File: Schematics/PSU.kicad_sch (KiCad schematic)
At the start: 59 parts

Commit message: - Updated current libraries - New 7 inc display with ESP32S3 and second USB upload port - Start of I2C feeder interface slave on display.
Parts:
- gave numbers to parts that had none: 59

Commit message: updated schematics.
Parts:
- J44: value Upper Cannon -> Upper Cannon
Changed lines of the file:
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@@
 			)
 		)
-		(property "Value" "Upper Cannon "
+		(property "Value" "Upper Cannon"
 			(at 190.5 22.86 90)
 			(effects

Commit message: Upgreade byte value interface to short.  First stage of refactoring midi input for rotory encoders.  Still needs scaling.
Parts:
- renumbered C67 to C115, C71 to C116, C64 to C117, C68 to C118, C72 to C119, C65 to C120, C69 to C121, C73 to C122, C66 to C123, C70 to C124, C74 to C125, D17 to D10, D13 to D11, D16 to D12, D19 to D13, D12 to D5, D15 to D6, D18 to D7, D11 to D8, D14 to D9, J44 to J55, J45 to J56, J46 to J57, J47 to J58, J48 to J59, J49 to J60, J50 to J61, J51 to J62, MES3 to MES2, MES6 to MES3, MES2 to MES4, MES4 to MES5, MES5 to MES6, R76 to R263, R77 to R264, RV3 to RV11, RV4 to RV12, RV5 to RV13, U23 to U73, U28 to U74, U34 to U75, U24 to U76, U26 to U77, U29 to U78, U31 to U79, U33 to U80, U35 to U81, U25 to U82, U27 to U83, U30 to U84, U32 to U85, U36 to U86

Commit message: Updated schematics including VCO and VCF daughter boards
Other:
- company:       MLE Tech                  Cedar Park, TX -> (none)
- title: Synth #2 -> Primary Power Supply
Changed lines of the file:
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@@
 	(paper "USLegal")
 	(title_block
-		(title "Synth #2")
-		(date "2023-07-27")
-		(rev "0.1")
-		(company "      MLE Tech                  Cedar Park, TX")
-		(comment 2 "In Development")
+		(title "Primary Power Supply")
+		(date "2025-01-16")
+		(rev "1.4")
+		(comment 1 "In Development ")
 	)
 	(junction

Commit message: Cleaned up page advance on display controls.
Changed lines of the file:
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@@
 (kicad_sch
-	(version 20231120)
+	(version 20250114)
 	(generator "eeschema")
-	(generator_version "8.0")
+	(generator_version "9.0")
 	(paper "USLegal")
 	(title_block
@@
 		(comment 1 "In Development ")
 	)
+	(text "Back Panel"
+		(exclude_from_sim no)
+		(at 35.3568 17.3482 0)
+		(effects
+			(font
+				(size 1.524 1.524)
+				(thickness 0.3048)
+				(bold yes)
+			)
+			(justify right bottom)
+		)
+	)
+	(text "LV300"
+		(exclude_from_sim no)
+		(at 30.48 83.185 0)
+		(effects
+			(font
+				(size 1.524 1.524)
+				(thickness 0.3048)
+				(bold yes)
+			)
+			(justify right bottom)
+		)
+	)
+	(text "Front Panel"
+		(exclude_from_sim no)
+		(at 162.56 53.34 0)
+		(effects
+			(font
+				(size 1.524 1.524)
+				(thickness 0.3048)
+				(bold yes)
+			)
+			(justify right bottom)
+		)
+	)
+	(text "Back Panel"
+		(exclude_from_sim no)
+		(at 210.82 17.78 0)
+		(effects
+			(font
+				(size 1.524 1.524)
+				(thickness 0.3048)
+				(bold yes)
+			)
+			(justify right bottom)
+		)
+	)
+	(text "Front Panel"
+		(exclude_from_sim no)
+		(at 257.81 60.96 0)
+		(effects
+			(font
+				(size 1.524 1.524)
+				(thickness 0.3048)
+				(bold yes)
+			)
+			(justify right bottom)
+		)
+	)
+	(text "LV30"
+		(exclude_from_sim no)
+		(at 30.4292 46.4566 0)
+		(effects
+			(font
+				(size 1.524 1.524)
+				(thickness 0.3048)
+				(bold yes)
+			)
+			(justify right bottom)
+		)
+	)
+	(text "Back Panel"
+		(exclude_from_sim no)
+		(at 97.6122 17.0942 0)
+		(effects
+			(font
+				(size 1.524 1.524)
+				(thickness 0.3048)
+				(bold yes)
+			)
+			(justify right bottom)
+		)
+	)
+	(text "LV300"
+		(exclude_from_sim no)
+		(at 30.1752 130.1496 0)
+		(effects
+			(font
+				(size 1.524 1.524)
+				(thickness 0.3048)
+				(bold yes)
+			)
+			(justify right bottom)
+		)
+	)
+	(text "Front Panel"
+		(exclude_from_sim no)
+		(at 61.8236 17.1196 0)
+		(effects
+			(font
+				(size 1.524 1.524)
+				(thickness 0.3048)
+				(bold yes)
+			)
+			(justify right bottom)
+		)
+	)
 	(junction
 		(at 77.47 161.29)
@@
 		)
 	)
-	(text "Back Panel"
-		(exclude_from_sim no)
-		(at 35.3568 17.3482 0)
-		(effects
-			(font
-				(size 1.524 1.524)
-				(thickness 0.3048)
-				(bold yes)
-			)
-			(justify right bottom)
-		)
-	)
-	(text "LV300"
-		(exclude_from_sim no)
-		(at 30.48 83.185 0)
-		(effects
-			(font
-				(size 1.524 1.524)
-				(thickness 0.3048)
-				(bold yes)
-			)
-			(justify right bottom)
-		)
-	)
-	(text "Front Panel"
-		(exclude_from_sim no)
-		(at 162.56 53.34 0)
-		(effects
-			(font
-				(size 1.524 1.524)
-				(thickness 0.3048)
-				(bold yes)
-			)
-			(justify right bottom)
-		)
-	)
-	(text "Back Panel"
-		(exclude_from_sim no)
-		(at 210.82 17.78 0)
-		(effects
-			(font
-				(size 1.524 1.524)
-				(thickness 0.3048)
-				(bold yes)
-			)
-			(justify right bottom)
-		)
-	)
-	(text "Front Panel"
-		(exclude_from_sim no)
-		(at 257.81 60.96 0)
-		(effects
-			(font
-				(size 1.524 1.524)
-				(thickness 0.3048)
-				(bold yes)
-			)
-			(justify right bottom)
-		)
-	)
-	(text "LV30"
-		(exclude_from_sim no)
-		(at 30.4292 46.4566 0)
-		(effects
-			(font
-				(size 1.524 1.524)
-				(thickness 0.3048)
-				(bold yes)
-			)
-			(justify right bottom)
-		)
-	)
-	(text "Back Panel"
-		(exclude_from_sim no)
-		(at 97.6122 17.0942 0)
-		(effects
-			(font
-				(size 1.524 1.524)
-				(thickness 0.3048)
-				(bold yes)
-			)
-			(justify right bottom)
-		)
-	)
-	(text "LV300"
-		(exclude_from_sim no)
-		(at 30.1752 130.1496 0)
-		(effects
-			(font
-				(size 1.524 1.524)
-				(thickness 0.3048)
-				(bold yes)
-			)
-			(justify right bottom)
-		)
-	)
-	(text "Front Panel"
-		(exclude_from_sim no)
-		(at 61.8236 17.1196 0)
-		(effects
-			(font
-				(size 1.524 1.524)
-				(thickness 0.3048)
-				(bold yes)
-			)
-			(justify right bottom)
-		)
-	)
 	(label "Brown"
 		(at 96.52 29.21 0)
-		(fields_autoplaced yes)
 		(effects
 			(font
@@
 	(label "+7.0v"
 		(at 168.9608 64.7446 180)
-		(fields_autoplaced yes)
 		(effects
 			(font
@@
 	(label "+15.0V"
 		(at 169.1894 104.0384 180)
-		(fields_autoplaced yes)
 		(effects
 			(font
@@
 	(label "gray"
 		(at 107.95 34.29 0)
-		(fields_autoplaced yes)
 		(effects
 			(font
@@
 	(label "Red"
 		(at 107.95 21.59 0)
-		(fields_autoplaced yes)
 		(effects
 			(font
@@
 	(label "Yellow"
 		(at 107.95 29.21 0)
-		(fields_autoplaced yes)
 		(effects
 			(font
@@
 	(label "-15.0V"
 		(at 169.0878 151.0792 180)
-		(fields_autoplaced yes)
 		(effects
 			(font
@@
 	(label "Orange"
 		(at 96.52 34.29 0)
-		(fields_autoplaced yes)
 		(effects
 			(font
@@
 	(label "Black"
 		(at 96.52 21.59 0)
-		(fields_autoplaced yes)
 		(effects
 			(font
@@
 	(label "Blue"
 		(at 107.95 26.67 0)
-		(fields_autoplaced yes)
 		(effects
 			(font
@@
 	(label "White"
 		(at 96.52 26.67 0)
-		(fields_autoplaced yes)
 		(effects
 			(font

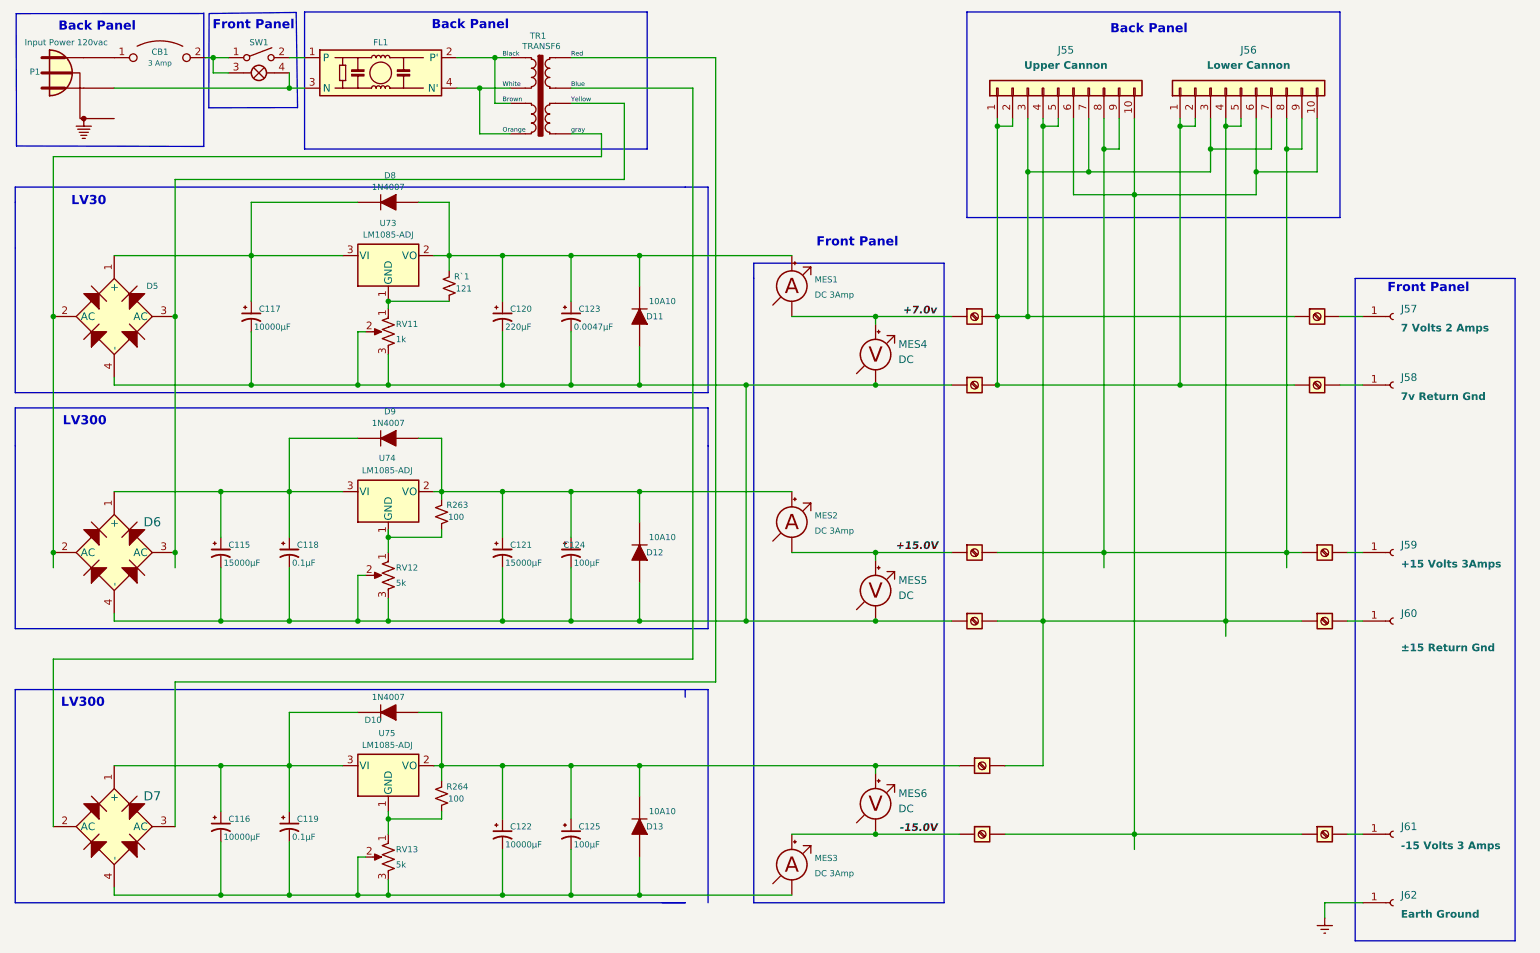
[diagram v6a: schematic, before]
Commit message: Fixed bugs in voice selection on configuration.  Reorganized schematics to have different master drawings for power and audio paths.  Started work on dual 3-pole state variable filter with resonance.
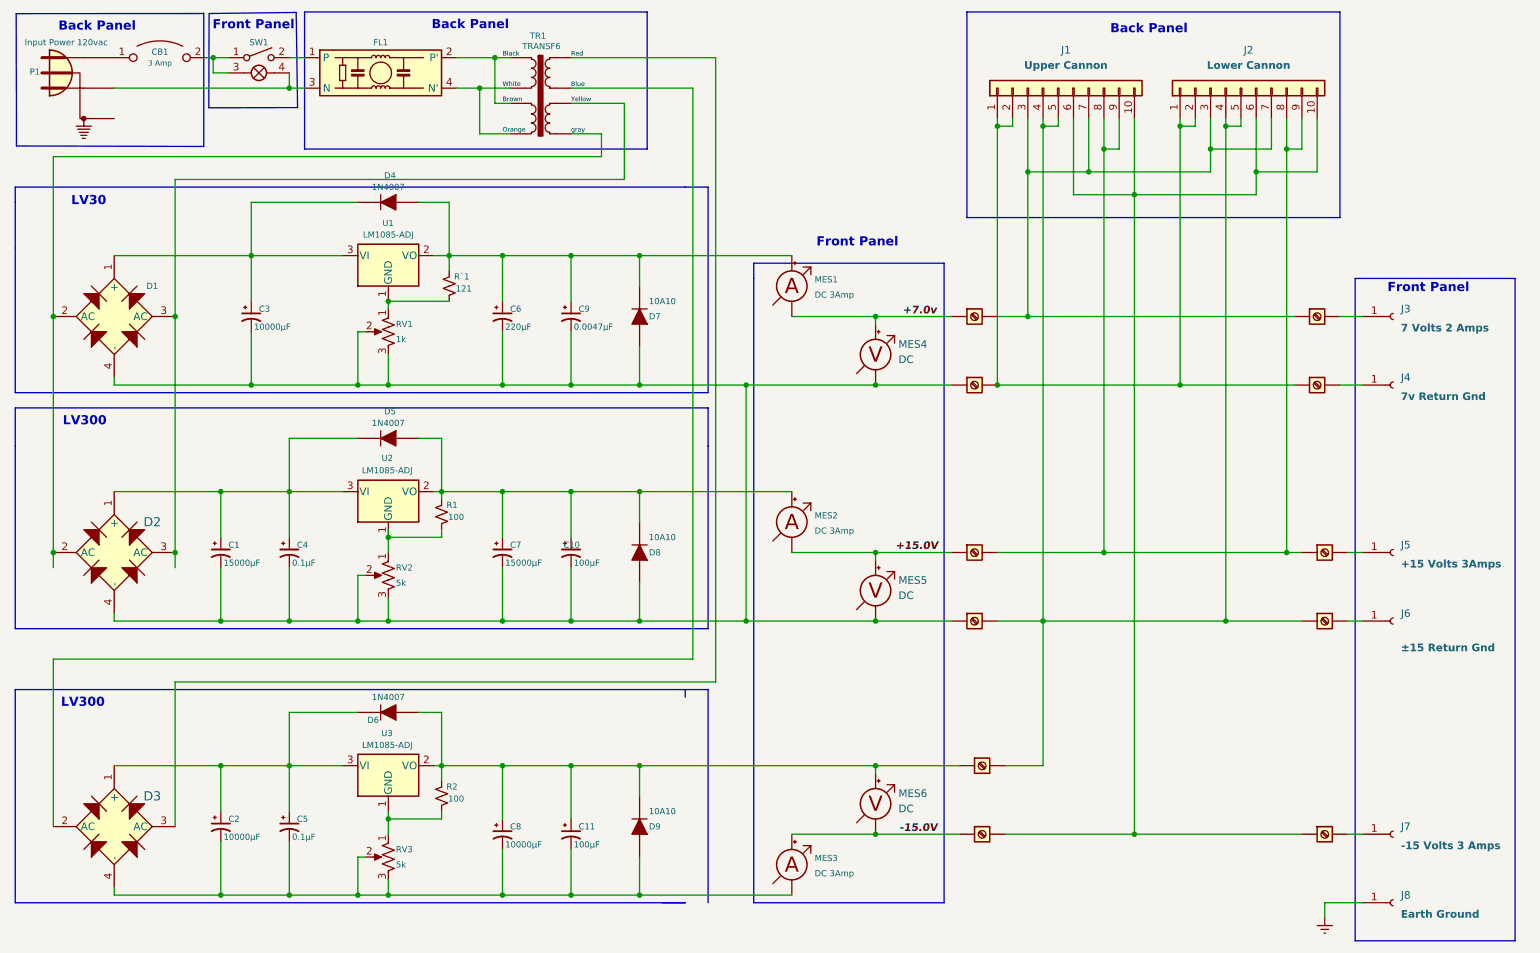
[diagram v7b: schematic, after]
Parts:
- renumbered C115 to C1, C124 to C10, C125 to C11, C116 to C2, C117 to C3, C118 to C4, C119 to C5, C120 to C6, C121 to C7, C122 to C8, C123 to C9, D5 to D1, D6 to D2, D7 to D3, D8 to D4, D9 to D5, D10 to D6, D11 to D7, D12 to D8, D13 to D9, J55 to J1, J56 to J2, J57 to J3, J58 to J4, J59 to J5, J60 to J6, J61 to J7, J62 to J8, R263 to R1, R264 to R2, RV11 to RV1, RV12 to RV2, RV13 to RV3, U73 to U1, U82 to U10, U83 to U11, U84 to U12, U85 to U13, U86 to U14, U74 to U2, U75 to U3, U76 to U4, U77 to U5, U78 to U6, U79 to U7, U80 to U8, U81 to U9
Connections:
- new net: J1.1 (Pin_1), J1.2 (Pin_2), J2.1 (Pin_1), J2.2 (Pin_2), U11., U5.
- new net: J1.3 (Pin_3), J1.7 (Pin_7), J2.3 (Pin_3), J2.7 (Pin_7), U10., U4.

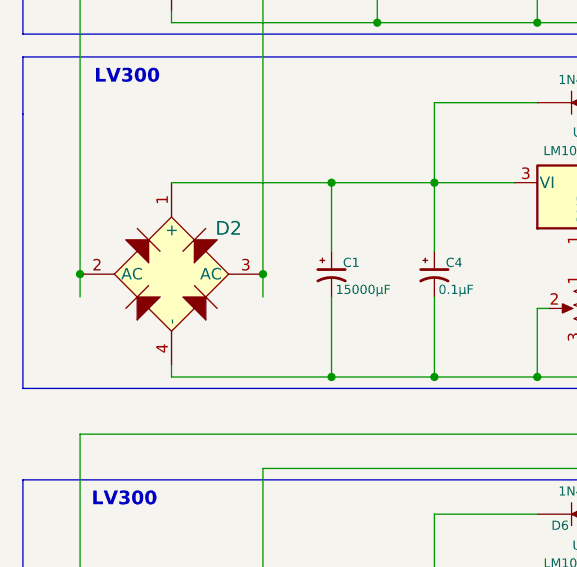
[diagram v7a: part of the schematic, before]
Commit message: Fixed schematic errors.
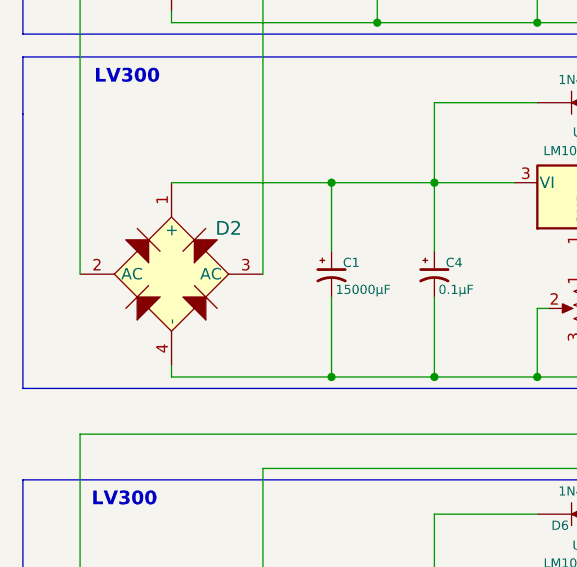
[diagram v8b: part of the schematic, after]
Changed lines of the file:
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@@
-	)
-	(junction
-		(at 21.59 104.14)
-		(diameter 0)
-		(color 0 0 0 0)
 	)
 	(junction
@@
 	)
 	(junction
-		(at 41.91 104.14)
-		(diameter 0)
-		(color 0 0 0 0)
-	)
-	(junction
 		(at 158.75 139.7)
 		(diameter 0)
@@
 	(wire
 		(pts
-			(xy 41.91 104.14) (xy 41.91 106.68)
-		)
-		(stroke
-			(width 0)
-			(type default)
-		)
-	)
-	(wire
-		(pts
 			(xy 158.75 140.97) (xy 158.75 139.7)
 		)
@@
 		)
 		(stroke
-			(width 0)
-			(type default)
-		)
-	)
-	(wire
-		(pts
-			(xy 21.59 104.14) (xy 21.59 106.68)
-		)
-		(stroke
